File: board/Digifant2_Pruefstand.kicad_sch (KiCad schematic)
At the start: 56 parts, among them J0 VW ECU HARNESS, J1 12V BENCH IN, J2 IDLE VALVE N71, J3 OLED / UI I2C, Q1 2N7002, Q2 P-MOS -30V >=5A, Q3 2N7002, Q5 2N7002, SW1 PUSH, SW2 PUSH, SW3 PUSH, U1 INA226 (0x40), U2 MCP4728 (0x60), U3 INA226 (0x41), U4 AD9833, U5 Raspberry Pi Pico, U6 TS5A3159A, U7 TS5A3159A, U8 TS5A3159A, Y1 25MHz

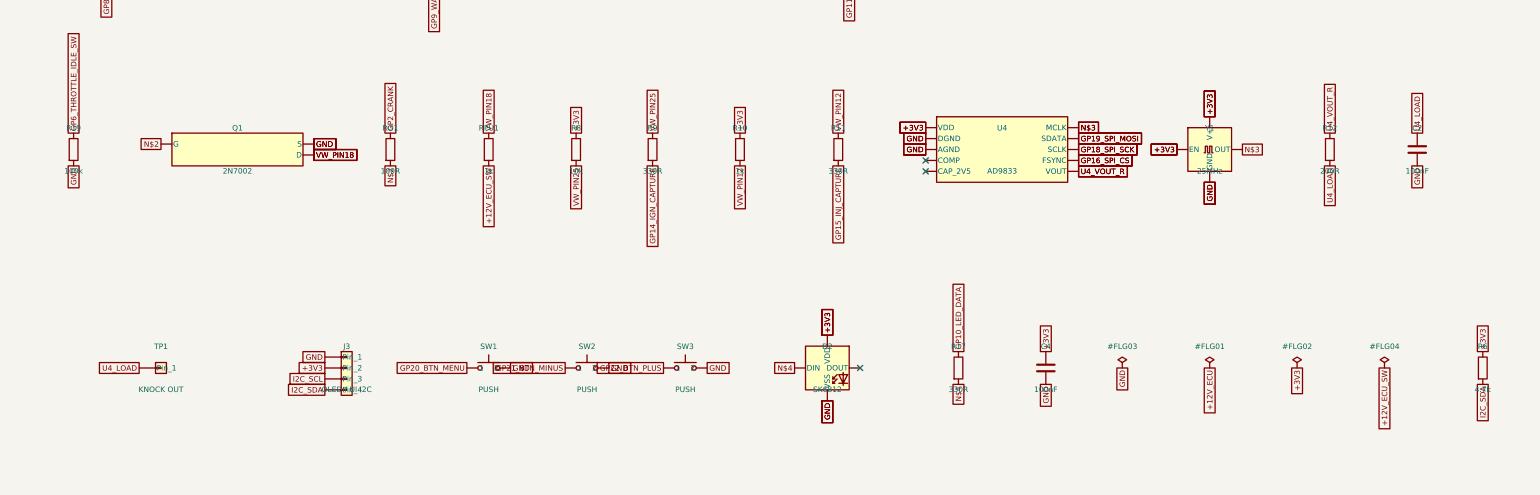
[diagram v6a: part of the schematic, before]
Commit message: Add missing AD9833 decoupling caps (C7, C8) before fab
The layout review flagged AD9833's COMP/CAP_2V5 pins as decoupling-only
with no cap ever added -- a real gap, not cosmetic, since skipping it
would mean a bodge-wire fix after fab. Added per ADI's recommended
application circuit: 100nF from each pin to AGND.

- digifant2_pruefstand.py: C7 (COMP) and C8 (CAP_2V5), both to gnd.
- Schematic: regenerated a scratch copy to get circuit-synth's correct
  net/label placement math, then spliced just the new symbol + label
  blocks into the committed schematic (preserving all prior manual
  work). Removed the two now-stale no_connect flags on U4's COMP/
  CAP_2V5 pins. Renamed the auto-generated net labels from circuit-
  synth's "N$4"/"N$5" to "U4_COMP"/"U4_CAP2V5" -- the board already had
  an unrelated net named "N$4" elsewhere, which collided.
- PCB: placed both caps by hand next to U4, in the same tightly-packed
  corner as the U1/U3/RS1/RS2 pocket. Both hot-side traces are routed
  and DRC-clean. C8's GND pad has one short unrouted line left -- this
  corner fights scripted routing exactly like that other pocket did,
  so it's left for the same quick manual finish in KiCad rather than
  more trial-and-error coordinate math.

Co-Authored-By: Claude Sonnet 5 <noreply@anthropic.com>
Claude-Session: https://claude.ai/code/session_01GgbvgUaRvNV7WyBdaSUkDT
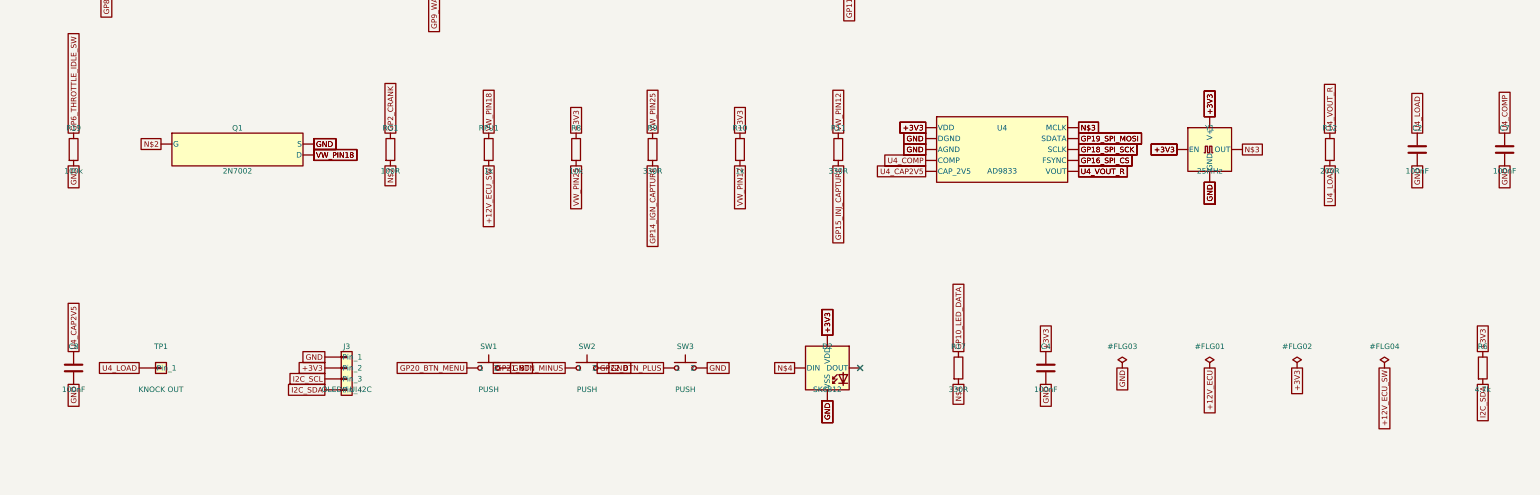
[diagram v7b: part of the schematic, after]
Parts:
- added C7, C8: 100nF, Capacitor_SMD:C_0805_2012Metric, symbol Device:C
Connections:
- net GND: now also C7.2, C8.2
- net U4_COMP: now reaches U4.1 (COMP)
- net U4_COMP: now also C7.1
- net U4_CAP2V5: now reaches U4.3 (CAP_2V5)
- net U4_CAP2V5: now also C8.1
- no-connect marks 22 -> 20
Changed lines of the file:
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@@
 		)
 	)
+		(symbol
+			(lib_id Device:C)
+			(at 370.84000000000003 259.08 0)
+			(in_bom yes)
+			(on_board yes)
+			(dnp no)
+			(property
+				"Reference"
+				"C7"
+				(at 370.84000000000003 254.07999999999998 0)
+				(effects
+					(font
+						(size 1.27 1.27)
+					)
+				)
+			)
+			(property
+				"Value"
+				"100nF"
+				(at 370.84000000000003 264.08 0)
+				(effects
+					(font
+						(size 1.27 1.27)
+					)
+				)
+			)
+			(property
+				"Footprint"
+				"Capacitor_SMD:C_0805_2012Metric"
+				(at 370.84000000000003 269.08 0)
+				(effects
+					(font
+						(size 1.27 1.27)
+					)
+					(hide yes)
+				)
+			)
+			(instances
+				(project
+					"circuit"
+					(path
+						"/"
+						(reference C7)
+						(unit 1)
+					)
+				)
+				(project
+					"/workspace/digifant2-pruefstand/digifant2_pruefstand_scratch_addcaps/digifant2_pruefstand_scratch_addcaps"
+					(path
+						"/096cc5cf-556d-44cb-bb18-6e4ad9bdecd8/1cb8be03-44d5-48c5-b2c4-df3d76afeeda"
+						(reference C7)
+						(unit 1)
+					)
+				)
+			)
+		)
+		(symbol
+			(lib_id Device:C)
+			(at 38.1 309.88 0)
+			(in_bom yes)
+			(on_board yes)
+			(dnp no)
+			(property
+				"Reference"
+				"C8"
+				(at 38.1 304.88 0)
+				(effects
+					(font
+						(size 1.27 1.27)
+					)
+				)
+			)
+			(property
+				"Value"
+				"100nF"
+				(at 38.1 314.88 0)
+				(effects
+					(font
+						(size 1.27 1.27)
+					)
+				)
+			)
+			(property
+				"Footprint"
+				"Capacitor_SMD:C_0805_2012Metric"
+				(at 38.1 319.88 0)
+				(effects
+					(font
+						(size 1.27 1.27)
+					)
+					(hide yes)
+				)
+			)
+			(instances
+				(project
+					"circuit"
+					(path
+						"/"
+						(reference C8)
+						(unit 1)
+					)
+				)
+				(project
+					"/workspace/digifant2-pruefstand/digifant2_pruefstand_scratch_addcaps/digifant2_pruefstand_scratch_addcaps"
+					(path
+						"/096cc5cf-556d-44cb-bb18-6e4ad9bdecd8/1cb8be03-44d5-48c5-b2c4-df3d76afeeda"
+						(reference C8)
+						(unit 1)
+					)
+				)
+			)
+		)
 	(global_label
 		VW_PIN2
@@
 	(no_connect (at 210.82 198.12))
 	(no_connect (at 220.98 309.88))
-	(no_connect (at 236.22 261.62))
-	(no_connect (at 236.22 264.16))
 	(no_connect (at 360.68 101.6))
+		(global_label
+			U4_COMP
+			(at 236.22 261.62 180)
+			(effects
+				(font
+					(size 1.27 1.27)
+				)
+				(justify right)
+			)
+		)
+		(global_label
+			U4_CAP2V5
+			(at 236.22 264.15999999999997 180)
+			(effects
+				(font
+					(size 1.27 1.27)
+				)
+				(justify right)
+			)
+		)
+		(global_label
+			U4_COMP
+			(at 370.84000000000003 255.26999999999998 90)
+			(effects
+				(font
+					(size 1.27 1.27)
+				)
+				(justify left)
+			)
+		)
+		(global_label
+			GND
+			(at 370.84000000000003 262.89 270)
+			(effects
+				(font
+					(size 1.27 1.27)
+				)
+				(justify right)
+			)
+		)
+		(global_label
+			U4_CAP2V5
+			(at 38.1 306.07 90)
+			(effects
+				(font
+					(size 1.27 1.27)
+				)
+				(justify left)
+			)
+		)
+		(global_label
+			GND
+			(at 38.1 313.69 270)
+			(effects
+				(font
+					(size 1.27 1.27)
+				)
+				(justify right)
+			)
+		)
 	(sheet_instances
 		(path

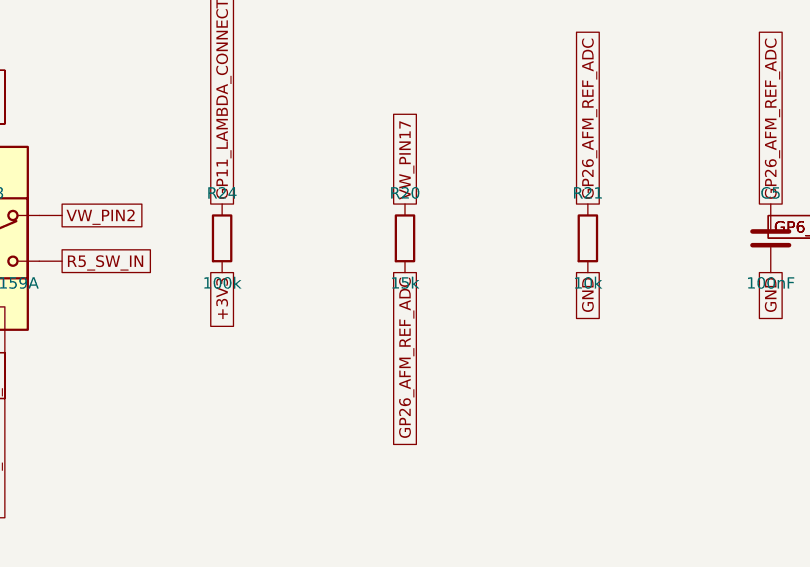
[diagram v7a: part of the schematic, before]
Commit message: Fix VW-17 divider headroom before fab: R20 15k -> 20k
Found in USE_CASES.md's verification pass: the divider's stated 9V
worst case (VW-17, airflow-pot reference) divided down to 3.6V through
the old 15k/10k ratio -- right at the RP2040 ADC's absolute-max input
rating, zero margin. Nominal 5V operation was always safe; it was
specifically that stated fault/worst-case voltage with no headroom.

R20 -> 20k changes the ratio from 10/25=0.4 to 10/30=0.333, so the same
9V worst case now lands at 3.0V (0.6V of real margin) while nominal 5V
still sits mid-range at 1.67V. Value-only change (same footprint, no
topology change), so no re-routing needed -- updated in the circuit
source, schematic, and PCB.

Co-Authored-By: Claude Sonnet 5 <noreply@anthropic.com>
Claude-Session: https://claude.ai/code/session_01XcEuUwwCT37oProAm8HYeY
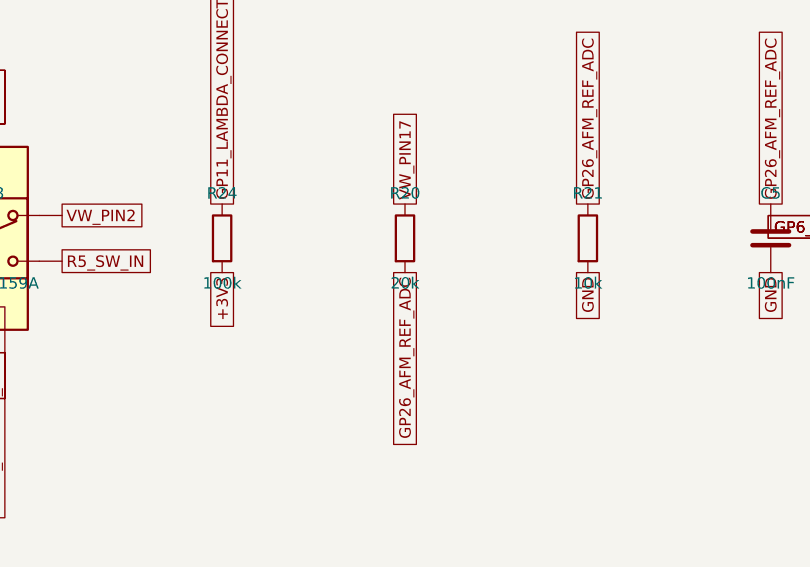
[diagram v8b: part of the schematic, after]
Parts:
- R20: value 15k -> 20k
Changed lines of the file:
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@@
 		(property
 			"Value"
-			"15k"
+			"20k"
 			(at 264.16 203.12 0)
 			(effects
